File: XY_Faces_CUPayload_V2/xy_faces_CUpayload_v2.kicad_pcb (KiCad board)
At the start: 4 copper layers, 76.3 x 98 mm, 33 parts, among them CN1 DF13A-5P-1.25H(21), CN2 DF13C-5P-1.25V(21), J2 Conn_01x01, J3 Conn_01x01, J4 Conn_01x01, J5 Conn_01x01, U1 VEML7700, U2 MCP9808_DFN, U3 DRV2605LDGS

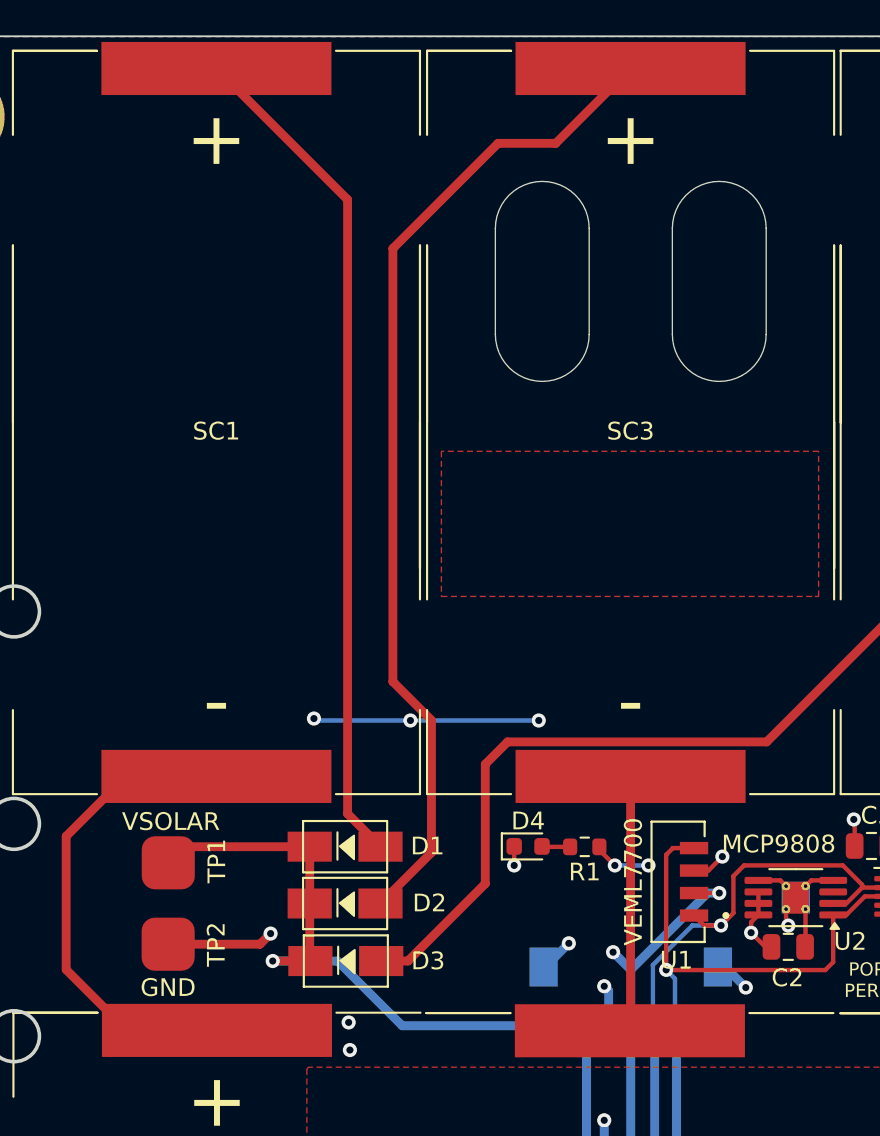
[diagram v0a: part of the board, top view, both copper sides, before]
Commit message: Created Camera Hole & Moved Diodes/Traces
VSolar pad unconnected
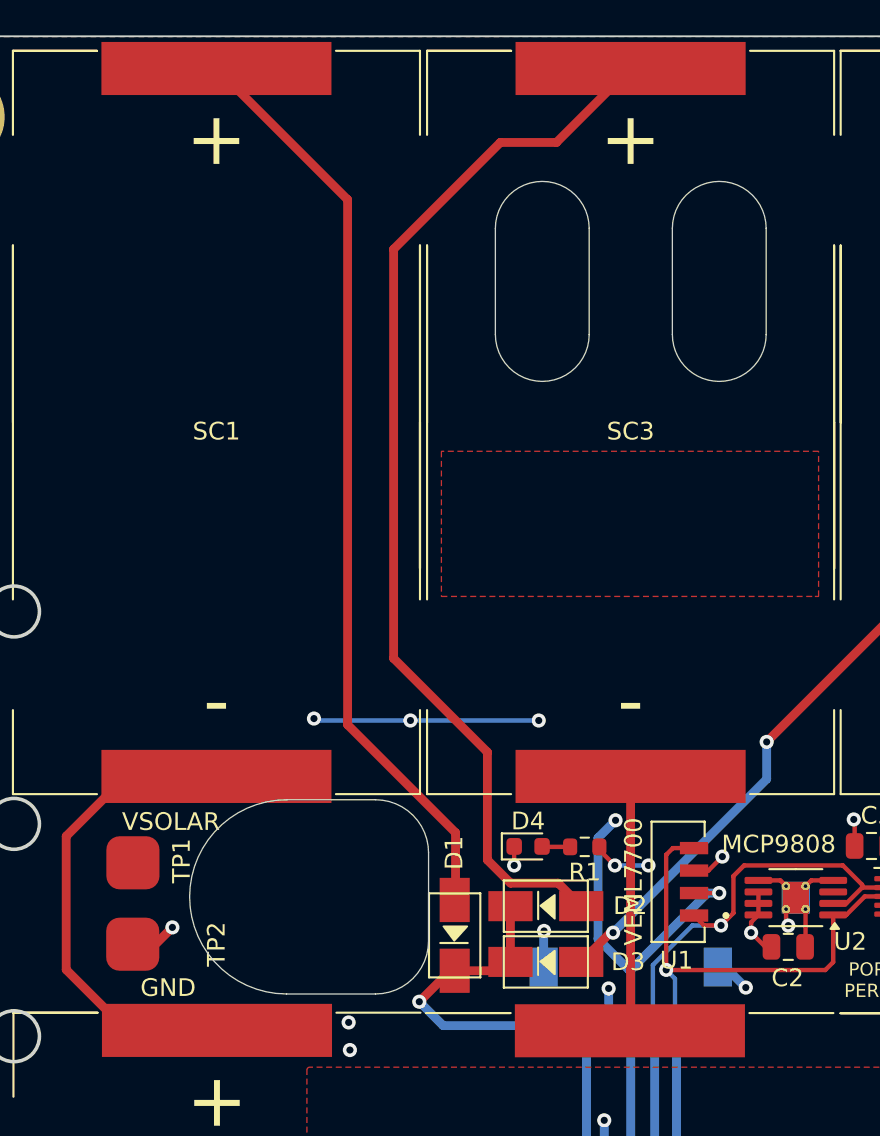
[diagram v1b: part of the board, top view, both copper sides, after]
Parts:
- moved D2 11.3 mm to (139.7, 114.9)
- moved D3 11.3 mm to (139.7, 118.0)
- moved D1 7.96 mm to (134.6, 116.5), turned to 90 degrees
- moved TP1 2.00 mm to (116.4, 112.5)
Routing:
- net VSOLAR: track 48.7 -> 31.8 mm
- net Net-(D3-A): track 75.4 -> 61.4 mm, vias 0 -> 2
- net +3V3: track 66.5 -> 74.7 mm
- net Net-(D1-A): track 47.8 -> 52.6 mm
- net GND: track 68.7 -> 65.2 mm
- net Net-(D2-A): track 56.7 -> 59.8 mm
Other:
- outline, holes or cut-outs redrawn
